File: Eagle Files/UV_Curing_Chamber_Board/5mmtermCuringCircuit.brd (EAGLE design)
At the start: 114.8 x 100 mm, 26 parts, among them IC1 7805T, IC2 L293D, T1 RFP30N06LE, T2 RFP30N06LE

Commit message: started cleaning up board sch and deleted old rev of board
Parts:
- removed MOTOR_A, MOTOR_B: (no value), SparkFun-Connectors:SCREWTERMINAL-5MM-2
- added MOTOR_BREAKOUT: (no value), con-lstb:MA04-1
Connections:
- net N$14: now also MOTOR_BREAKOUT.4; no longer MOTOR_A.2
- net N$15: now also MOTOR_BREAKOUT.3; no longer MOTOR_A.1
- net N$27: now also MOTOR_BREAKOUT.1; no longer MOTOR_B.1
- net N$28: now also MOTOR_BREAKOUT.2; no longer MOTOR_B.2

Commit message: schematic
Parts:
- moved MOTOR_BREAKOUT 110.6 mm to (31.8, 94.0)
- moved R4 2.54 mm to (16.5, 73.7)
- moved R3 2.54 mm to (50.8, 73.7), turned to 180 degrees
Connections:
- removed net N$1: C1.1, C3.+, IC1.3, IC2.16, R3.2, U$1.19
- removed net N$30: IC2.10, U$1.12
- removed net N$5 (its old number): R1.2, T2.1, U$1.8
- new net N$2: IC2.15, U$1.12
- net N$14: now also C1.1, C3.+, IC1.3, IC2.16, R1.2, R3.2, T2.1, U$1.19, U$1.8
- net N$29: now also IC2.10; no longer IC2.15
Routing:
- net 12V: track 377.6 -> 0.00 mm
- net N$14: track 31.0 -> 204.3 mm
- net N$1: track 133.7 -> 0.00 mm
- net N$5 (its old number): track 59.2 -> 0.00 mm
- net N$29: track 58.1 -> 0.00 mm
- net N$30: track 56.4 -> 0.00 mm
- net N$12: track 21.9 -> 0.77 mm
- net N$27: track 28.5 -> 43.0 mm
- net N$31: track 16.5 -> 14.1 mm
- net N$28: track 37.7 -> 40.1 mm, vias 0 -> 1

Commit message: board updates
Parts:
- moved C3 1.27 mm to (49.5, 63.5)
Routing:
- net N$14: track 204.3 -> 235.5 mm, vias 0 -> 2
- net N$12: track 0.77 -> 23.2 mm
- net N$28: track 40.1 -> 43.2 mm, vias 1 -> 2

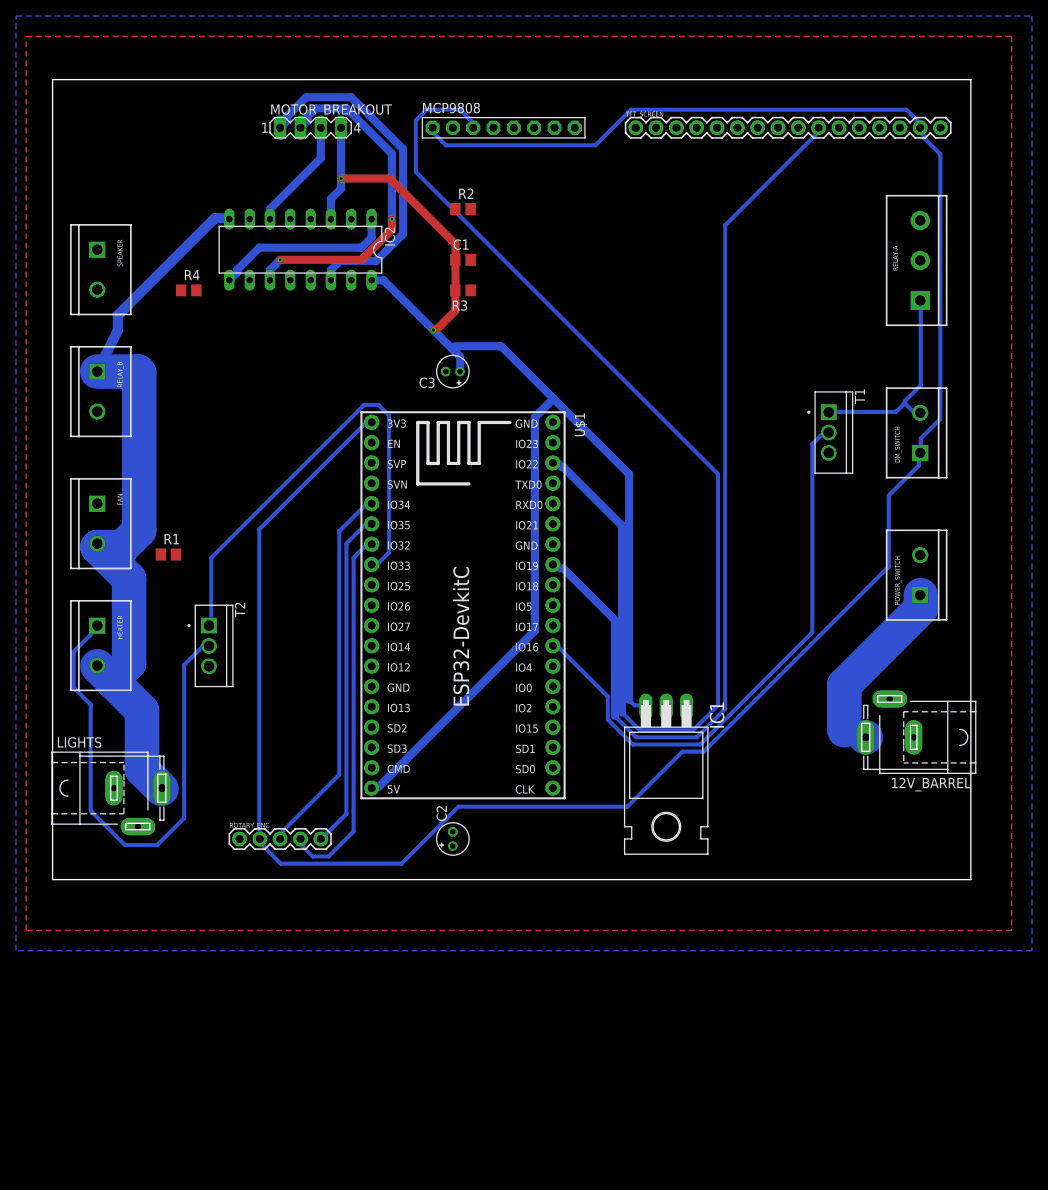
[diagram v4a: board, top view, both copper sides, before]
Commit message: removed unnecesary files
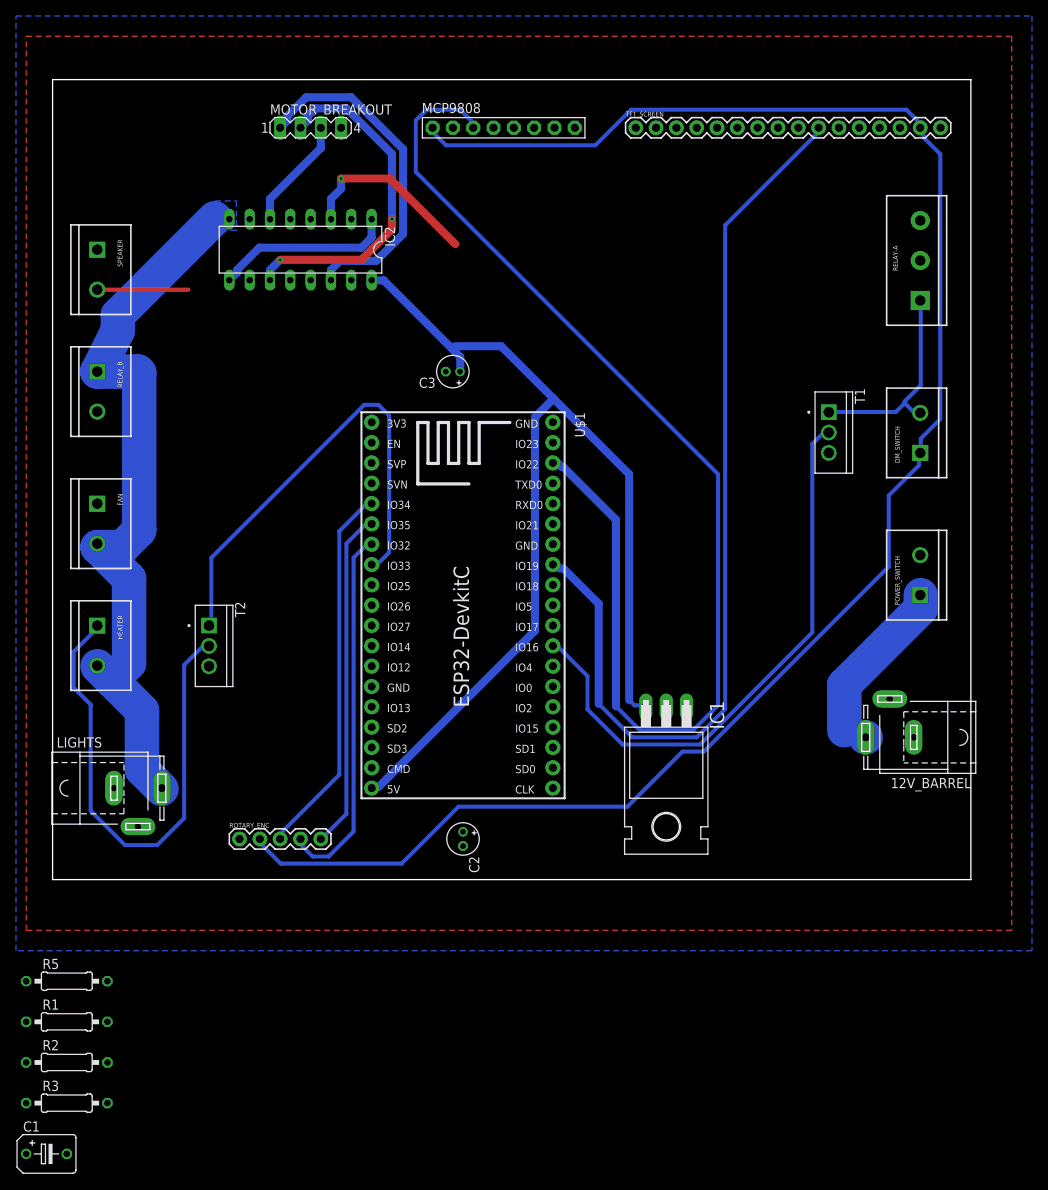
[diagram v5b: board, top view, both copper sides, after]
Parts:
- removed R4: 220, rcl:R0805
- added R5: 10k, rcl:0207/10
- C1: value 0.1uF -> .1uF; device rcl:C0805 -> rcl:B45181B
- R1: value 10K -> 220; device rcl:R0805 -> rcl:0207/10
- R2: value 10K -> 10k; device rcl:R0805 -> rcl:0207/10
- R3: device rcl:R0805 -> rcl:0207/10
- moved C1 123.3 mm to (-1.27, -34.3)
- moved R2 117.6 mm to (1.27, -22.9)
- moved R3 113.0 mm to (1.27, -27.9), turned to 0 degrees
- moved R1 59.8 mm to (1.27, -17.8)
- moved C2 1.27 mm to (50.8, 5.08), turned to 270 degrees
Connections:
- net N$7 renamed +3V3
- removed net N$14: C1.1, C3.+, IC1.3, IC2.16, IC2.3, MOTOR_BREAKOUT.4, R1.2, R3.2, T2.1, U$1.19, U$1.8
- new net +5V: C1.+, C3.+, IC1.3, IC2.16, IC2.3, MOTOR_BREAKOUT.4, R1.2, R5.2, RELAY_B.2, T2.1, U$1.19, U$1.8
- net 12V: no longer RELAY_B.2
- net GND: now also C1.-, R5.1; no longer C1.2, R1.1
- net N$17: now also R1.1; no longer R3.1
- net N$21: now also TFT_SCREEN.12, TFT_SCREEN.13, TFT_SCREEN.14
- net N$26: now also R3.1; no longer R4.1
- net N$6: now also R3.2; no longer R4.2
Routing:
- net N$14: track 235.5 -> 0.00 mm, vias 2 -> 0
- net +5V: track 0.00 -> 217.0 mm, vias 0 -> 1
- net +3V3: track 277.9 -> 218.6 mm
- net N$6: track 0.00 -> 11.4 mm
- net N$9: track 71.2 -> 72.0 mm
- added copper zone on layer 16, net RELAY_NO

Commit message: more unfucking schematic
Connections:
- net N$21: no longer TFT_SCREEN.12, TFT_SCREEN.13, TFT_SCREEN.14
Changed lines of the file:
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@@
 <contactref element="IC2" pad="12"/>
 <contactref element="U$1" pad="32"/>
-<contactref element="U$1" pad="38"/>
 <contactref element="U$1" pad="14"/>
 <polygon width="0.1524" layer="16">
@@
 <contactref element="R5" pad="1"/>
 <contactref element="C1" pad="-"/>
+<contactref element="TFT_SCREEN" pad="1"/>
+<contactref element="U$1" pad="38"/>
 <contactref element="MCP9808" pad="2"/>
-<contactref element="TFT_SCREEN" pad="1"/>
 <wire x1="107.95" y1="82.39" x2="110.49" y2="93.98" width="0" layer="19" extent="1-1"/>
 <wire x1="96.52" y1="53.34" x2="107.95" y2="82.39" width="0" layer="19" extent="1-1"/>
@@
 </signal>
 <signal name="N$10">
-<contactref element="MCP9808" pad="3"/>
 <contactref element="U$1" pad="36"/>
 <wire x1="52.0065" y1="94.6785" x2="52.0065" y2="94.01175" width="0.508" layer="16"/>
@@
 <wire x1="62.6745" y1="52.0065" x2="63.119" y2="51.562" width="1.016" layer="16"/>
 <wire x1="62.23" y1="52.0065" x2="62.6745" y2="52.0065" width="1.016" layer="16"/>
-<wire x1="52.0065" y1="94.01175" x2="52.07" y2="93.98" width="0.508" layer="16"/>
 <wire x1="62.23" y1="52.0065" x2="62.03" y2="52.08" width="1.016" layer="16"/>
+<contactref element="MCP9808" pad="3"/>
+<wire x1="52.0065" y1="94.01175" x2="52.07" y2="93.98" width="0" layer="19" extent="16-16"/>
 </signal>
 <signal name="N$11">
+<contactref element="U$1" pad="33"/>
 <contactref element="MCP9808" pad="4"/>
-<contactref element="U$1" pad="33"/>
 <wire x1="62.03" y1="44.46" x2="54.61" y2="93.98" width="0" layer="19" extent="1-1"/>
 </signal>
@@
 </signal>
 <signal name="N$21">
+<contactref element="U$1" pad="28"/>
 <contactref element="TFT_SCREEN" pad="11"/>
-<contactref element="U$1" pad="28"/>
-<contactref element="TFT_SCREEN" pad="12"/>
-<contactref element="TFT_SCREEN" pad="13"/>
-<contactref element="TFT_SCREEN" pad="14"/>
-<wire x1="102.87" y1="93.98" x2="105.41" y2="93.98" width="0" layer="19" extent="1-1"/>
-<wire x1="100.33" y1="93.98" x2="102.87" y2="93.98" width="0" layer="19" extent="1-1"/>
-<wire x1="97.79" y1="93.98" x2="100.33" y2="93.98" width="0" layer="19" extent="1-1"/>
 <wire x1="62.03" y1="31.76" x2="97.79" y2="93.98" width="0" layer="19" extent="1-1"/>
 </signal>
@@
 <wire x1="95.123" y1="93.7895" x2="95.25" y2="93.98" width="0.508" layer="16"/>
 <wire x1="62.23" y1="39.5605" x2="62.03" y2="39.38" width="1.016" layer="16"/>
-</signal>
-<signal name="N$23">
-<contactref element="TFT_SCREEN" pad="9"/>
-<contactref element="U$1" pad="37"/>
-<wire x1="62.03" y1="54.62" x2="92.71" y2="93.98" width="0" layer="19" extent="1-1"/>
 </signal>
 <signal name="N$24">
@@
 </signal>
 <signal name="N$29">
+<contactref element="IC2" pad="10"/>
 <contactref element="U$1" pad="15"/>
-<contactref element="IC2" pad="10"/>
 <wire x1="39.38" y1="21.6" x2="24.13" y2="74.93" width="0" layer="19" extent="1-1"/>
 </signal>
@@
 </signal>
 <signal name="N$5">
+<contactref element="IC2" pad="7"/>
 <contactref element="U$1" pad="11"/>
-<contactref element="IC2" pad="7"/>
 <wire x1="39.38" y1="31.76" x2="24.13" y2="82.55" width="0" layer="19" extent="1-1"/>
 </signal>
@@
 </signal>
 <signal name="N$12">
-<contactref element="U$1" pad="13"/>
 <contactref element="IC2" pad="1"/>
 <contactref element="IC2" pad="9"/>
@@
 <wire x1="39.37" y1="80.264" x2="39.37" y2="82.55" width="1.016" layer="16"/>
 <wire x1="25.3424125" y1="78.994" x2="38.1" y2="78.994" width="1.016" layer="16"/>
+<contactref element="U$1" pad="13"/>
 <wire x1="39.38" y1="26.68" x2="21.59" y2="74.93" width="0" layer="19" extent="1-1"/>
 </signal>
 <signal name="N$2">
+<contactref element="U$1" pad="12"/>
 <contactref element="IC2" pad="15"/>
-<contactref element="U$1" pad="12"/>
 <wire x1="39.38" y1="29.22" x2="36.83" y2="74.93" width="0" layer="19" extent="1-1"/>
 </signal>
@@
 <contactref element="C3" pad="+"/>
 <contactref element="IC1" pad="3"/>
-<contactref element="U$1" pad="19"/>
 <contactref element="U$1" pad="8"/>
-<contactref element="C1" pad="+"/>
 <wire x1="40.22725" y1="39.5605" x2="39.5605" y2="39.5605" width="0.508" layer="16"/>
 <wire x1="41.56075" y1="40.894" x2="40.22725" y2="39.5605" width="0.508" layer="16"/>
@@
 <wire x1="50.45075" y1="65.3415" x2="50.45075" y2="63.53175" width="1.016" layer="16"/>
 <contactref element="R1" pad="2"/>
+<contactref element="U$1" pad="19"/>
+<contactref element="C1" pad="+"/>
 <wire x1="35.56" y1="87.63" x2="35.56" y2="93.98" width="0" layer="19" extent="1-1"/>
 <wire x1="39.37" y1="74.93" x2="34.29" y2="82.55" width="0" layer="19" extent="1-1"/>
@@
 <wire x1="39.38" y1="57.16" x2="48.67275" y2="91.78925" width="0" layer="19" extent="16-16"/>
 </signal>
+<signal name="N$1">
+<contactref element="TFT_SCREEN" pad="9"/>
+<contactref element="U$1" pad="37"/>
+<wire x1="62.03" y1="54.62" x2="92.71" y2="93.98" width="0" layer="19" extent="1-1"/>
+</signal>
 </signals>
